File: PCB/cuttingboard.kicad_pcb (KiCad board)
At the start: 2 copper layers, 21 x 51 mm, 37 parts, among them J1 USB_C_Receptacle_USB2.0_14P, J2 Conn_01x20, J3 Conn_01x20, J4 Conn_01x03, SW1 SW_Push, U1 RP2040, U3 W25Q128JVS, U4 MCP1700x-330xxTT, Y1 12 MHz

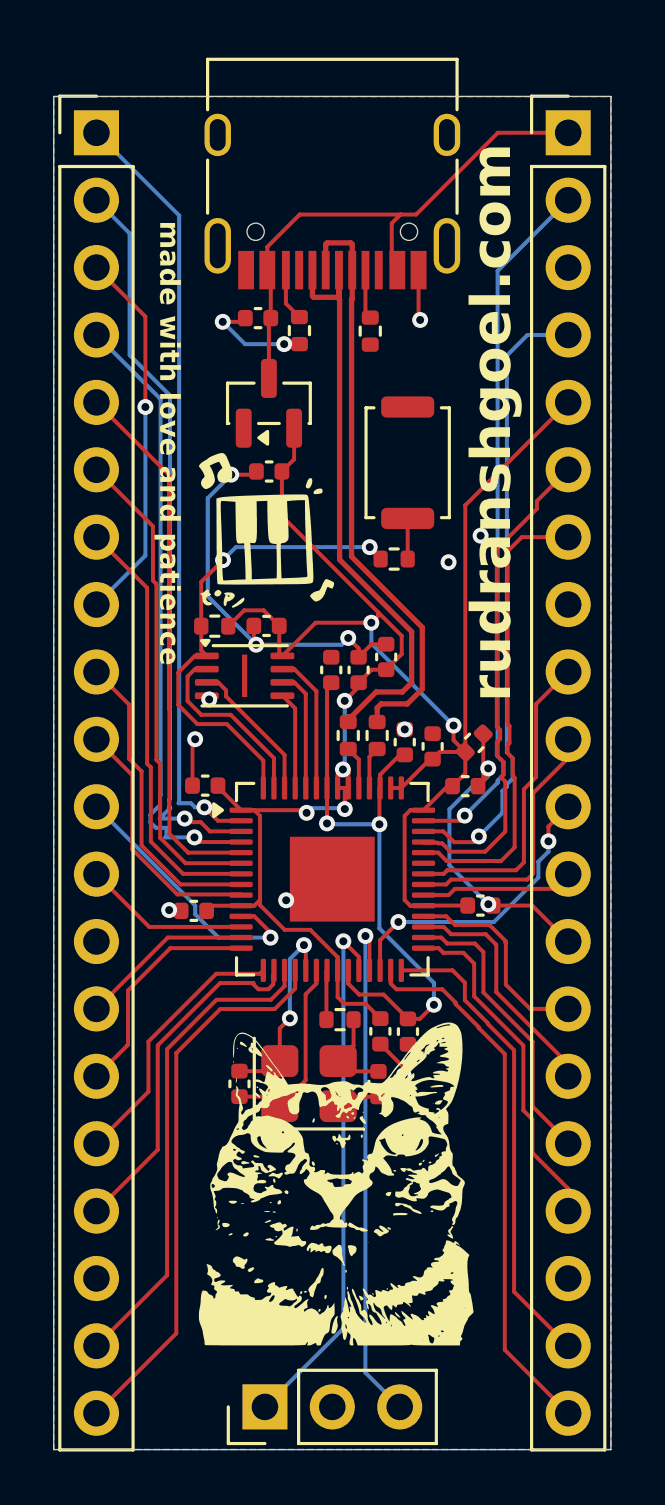
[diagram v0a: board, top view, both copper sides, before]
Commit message: updated devboard to new thing, added Accelerometer
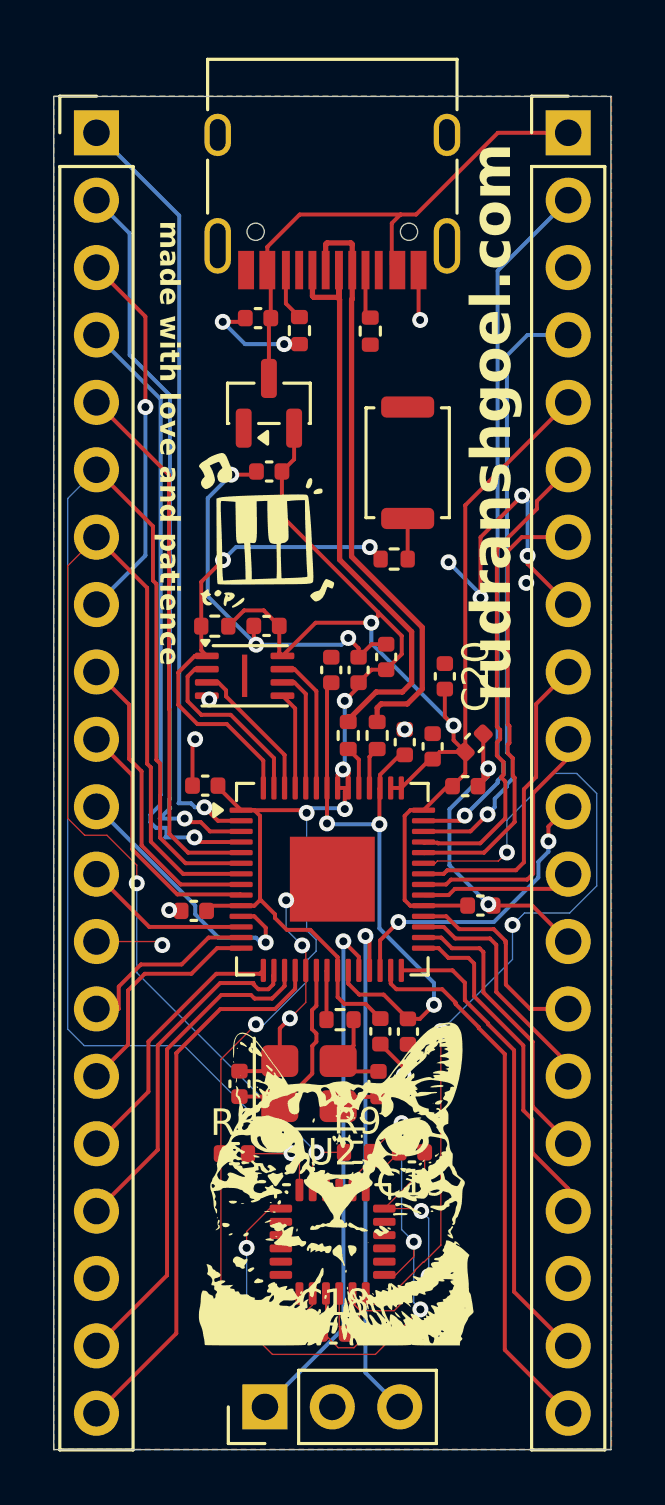
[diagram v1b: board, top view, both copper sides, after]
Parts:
- added C18: 0.1uF, Capacitor_SMD:C_0402_1005Metric, F.Cu at (102.3, 104.4)
- added C19: 2.2nf, Capacitor_SMD:C_0402_1005Metric, F.Cu at (105.3, 97.6)
- added C20: 0.1uF, Capacitor_SMD:C_0402_1005Metric, F.Cu at (106.5, 79.6)
- added R8: 4.7k, Resistor_SMD:R_0402_1005Metric, F.Cu at (98.6, 97.6)
- added R9: 4.7k, Resistor_SMD:R_0402_1005Metric, F.Cu at (103.2, 97.6)
- added U2: MPU-6050, Sensor_Motion:InvenSense_QFN-24_4x4mm_P0.5mm, F.Cu at (102.3, 100.9)
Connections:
- U1 pad 37: unconnected-(U1-GPIO25-Pad37) -> GPIO25
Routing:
- net +3V3: track 79.8 -> 126.1 mm, vias 6 -> 10
- net GND: track 61.4 -> 100.9 mm, vias 19 -> 27
- net GPIO4: track 18.3 -> 53.4 mm, vias 0 -> 1
- net GPIO25: track 0.00 -> 33.5 mm, vias 0 -> 3
- net GPIO5: track 16.2 -> 46.8 mm, vias 0 -> 2
- net Net-(U2-CPOUT): track 0.00 -> 2.60 mm
- net Net-(U2-REGOUT): track 0.00 -> 1.62 mm
- net GPIO26_ADC0: track 17.6 -> 16.8 mm
- net GPIO28_ADC2: track 23.7 -> 23.1 mm
- net GPIO27_ADC1: track 18.6 -> 18.1 mm

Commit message: added firmware and updated pcb files
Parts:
- added D1: LED, LED_SMD:LED_0805_2012Metric_Pad1.15x1.40mm_HandSolder, F.Cu at (97.1, 69.7)
- added R10: 1K, Resistor_SMD:R_0402_1005Metric, F.Cu at (97.2, 66.8)
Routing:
- net GPIO0: track 29.2 -> 37.9 mm
- net Net-(D1-A): track 0.00 -> 1.40 mm
